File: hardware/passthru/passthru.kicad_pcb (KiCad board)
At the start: 2 copper layers, 63.5 x 59.7 mm, 83 parts, among them J1 ARM_SWD, J2 RJ45_LED_Shielded, J3 Screw_Terminal_01x02, Q1 Q_PMOS_DGS, Q2 Q_PMOS_DGS, Q3 Q_NPN_BEC, U1 EFM32GG11B8xx, U2 KSZ8081RND, U3 LM5085, U4 TPS2375-1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

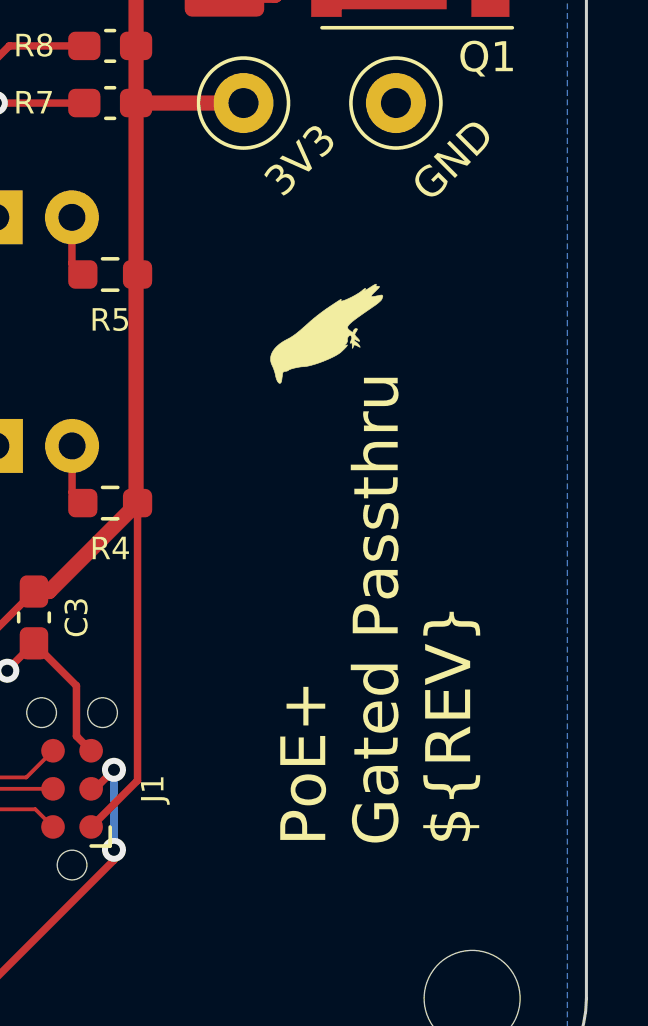
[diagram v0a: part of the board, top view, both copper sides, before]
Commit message: passthru: add pre-release revision to board
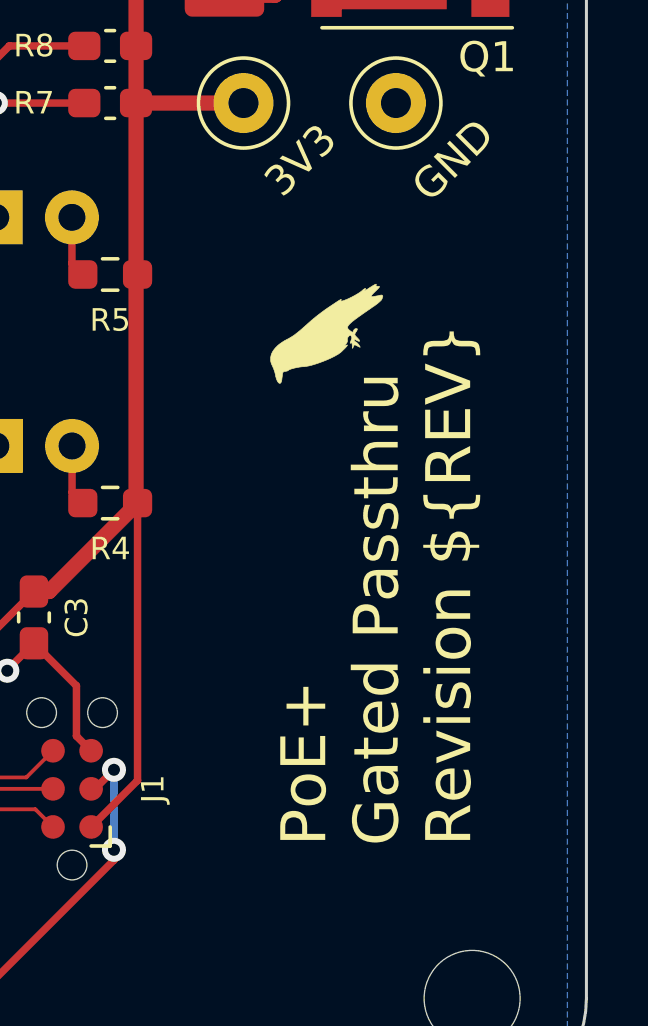
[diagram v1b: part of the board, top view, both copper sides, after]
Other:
- board text added: "PoE+ Gated Passthru Revision ${REV}"
- board text removed: "PoE+ Gated Passthru ${REV}"
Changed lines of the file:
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@@
     )
   )
+  (property "REV" "A-dev")
   (net 0 "")
   (net 1 "VDDA")
@@
     (effects (font (size 1 1) (thickness 0.2)) (justify mirror))
   )
-  (gr_text "PoE+\nGated Passthru\n${REV}" (at 170.815 112.395 90) (layer "F.SilkS")
+  (gr_text "PoE+\nGated Passthru\nRevision ${REV}" (at 170.815 112.395 90) (layer "F.SilkS")
     (effects (font (size 1.5 1.5) (thickness 0.3)) (justify left))
   )

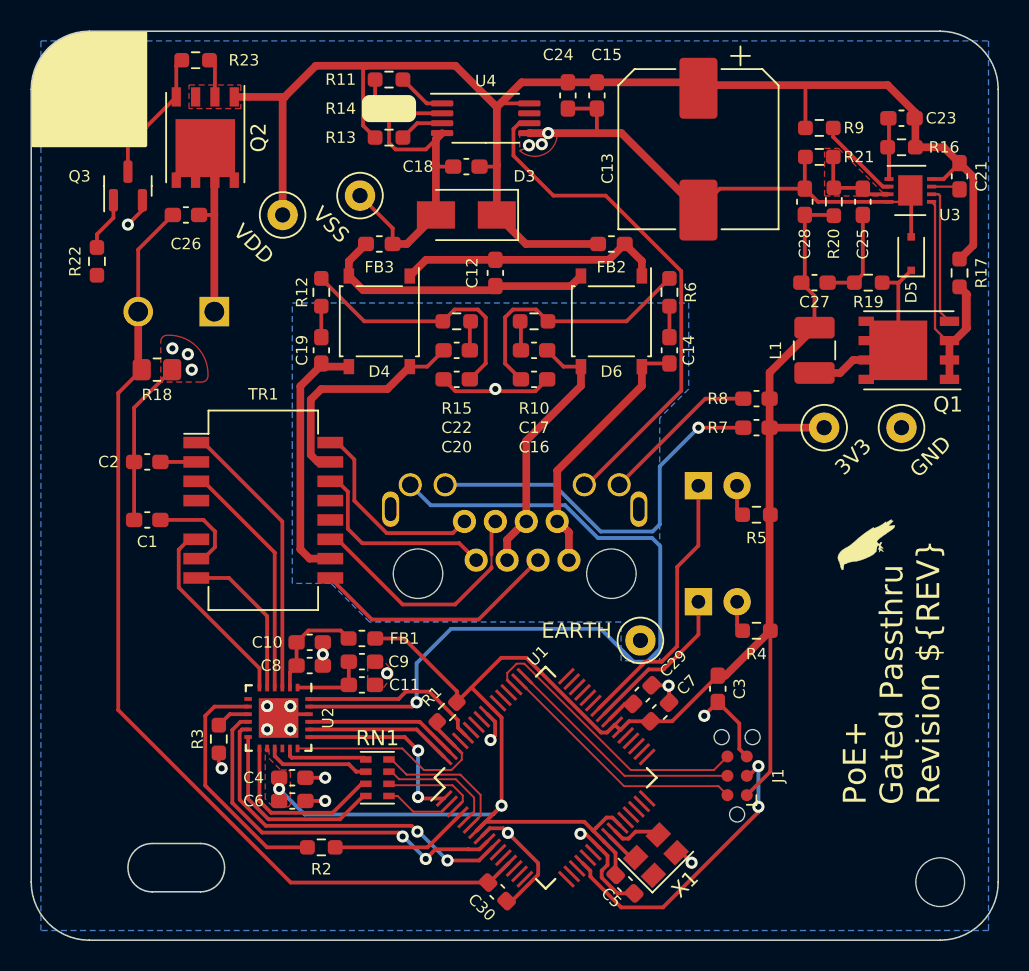
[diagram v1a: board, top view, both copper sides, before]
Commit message: passthru: finalize production parameters
I also spaced out the VDD rail a bit further.
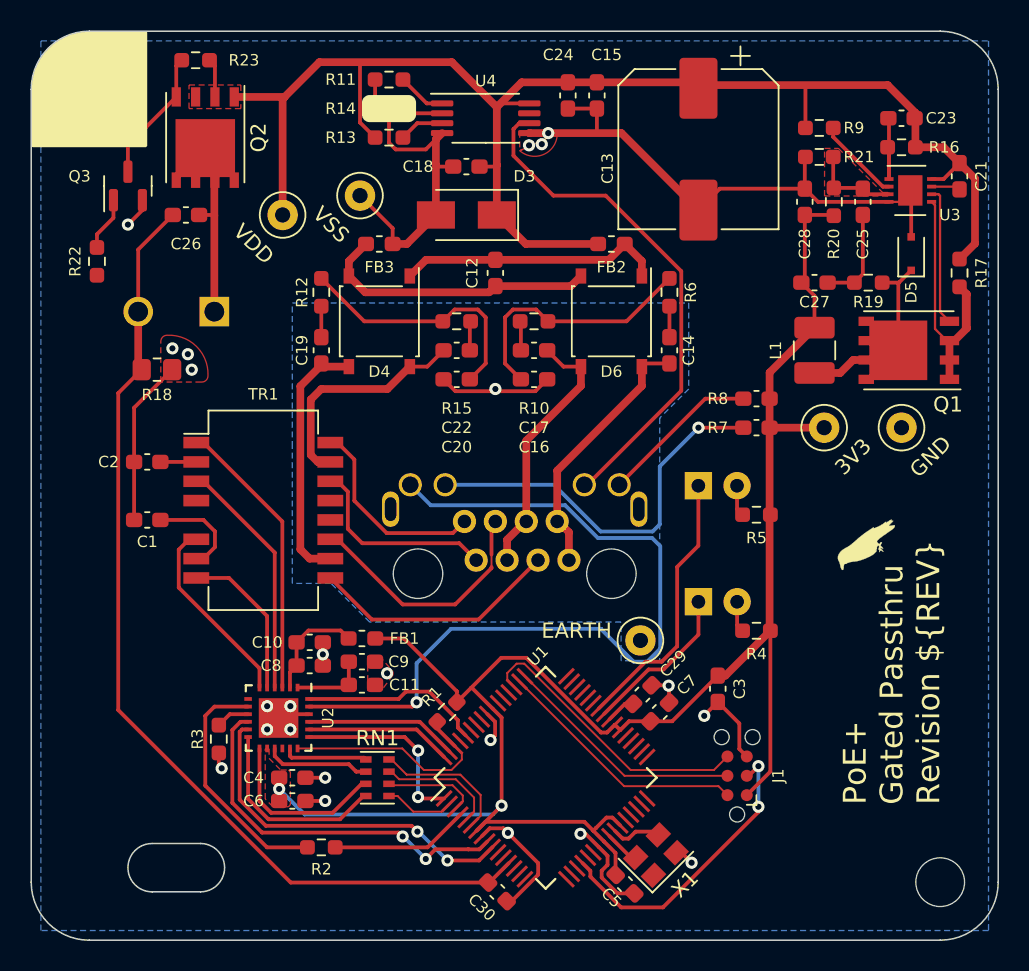
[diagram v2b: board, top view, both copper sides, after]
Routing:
- net VDD: track 99.7 -> 99.1 mm
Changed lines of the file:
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@@
 (kicad_pcb (version 20211014) (generator pcbnew)
   (general
-    (thickness 1.6)
+    (thickness 1.69)
   )
   (paper "A4")
@@
   (setup
     (stackup
-      (layer "F.SilkS" (type "Top Silk Screen"))
+      (layer "F.SilkS" (type "Top Silk Screen") (color "White"))
       (layer "F.Paste" (type "Top Solder Paste"))
-      (layer "F.Mask" (type "Top Solder Mask") (thickness 0.01))
+      (layer "F.Mask" (type "Top Solder Mask") (color "#0C4AD9D4") (thickness 0.01))
       (layer "F.Cu" (type "copper") (thickness 0.035))
-      (layer "dielectric 1" (type "core") (thickness 1.51) (material "FR4") (epsilon_r 4.5) (loss_tangent 0.02))
+      (layer "dielectric 1" (type "core") (thickness 1.6) (material "FR4") (epsilon_r 4.5) (loss_tangent 0.02))
       (layer "B.Cu" (type "copper") (thickness 0.035))
-      (layer "B.Mask" (type "Bottom Solder Mask") (thickness 0.01))
+      (layer "B.Mask" (type "Bottom Solder Mask") (color "#0C4AD9D4") (thickness 0.01))
       (layer "B.Paste" (type "Bottom Solder Paste"))
-      (layer "B.SilkS" (type "Bottom Silk Screen"))
+      (layer "B.SilkS" (type "Bottom Silk Screen") (color "White"))
       (copper_finish "None")
       (dielectric_constraints no)
@@
   (segment (start 139.16 77.67) (end 140.2225 76.6075) (width 0.508) (layer "F.Cu") (net 1))
   (segment (start 154.4 76.69) (end 153.275 75.565) (width 0.508) (layer "F.Cu") (net 1))
-  (segment (start 144.5107 78.6018) (end 144.78 78.3325) (width 0.508) (layer "F.Cu") (net 2))
   (segment (start 149.7375 78.3325) (end 150.4 77.67) (width 0.508) (layer "F.Cu") (net 2))
-  (segment (start 136.0918 78.6018) (end 144.5107 78.6018) (width 0.508) (layer "F.Cu") (net 2))
+  (segment (start 135.16 77.67) (end 136.23 78.74) (width 0.508) (layer "F.Cu") (net 2))
   (segment (start 135.16 76.69) (end 136.285 75.565) (width 0.508) (layer "F.Cu") (net 2))
   (segment (start 144.78 78.3325) (end 149.7375 78.3325) (width 0.508) (layer "F.Cu") (net 2))
   (segment (start 135.16 77.67) (end 135.16 76.69) (width 0.508) (layer "F.Cu") (net 2))
-  (segment (start 135.16 77.67) (end 136.0918 78.6018) (width 0.508) (layer "F.Cu") (net 2))
+  (segment (start 136.23 78.74) (end 144.3725 78.74) (width 0.508) (layer "F.Cu") (net 2))
+  (segment (start 144.3725 78.74) (end 144.78 78.3325) (width 0.508) (layer "F.Cu") (net 2))
   (segment (start 152.146 116.336876) (end 151.75875 116.724126) (width 0.25) (layer "F.Cu") (net 3))
   (segment (start 144.760877 107.842123) (end 144.4625 108.1405) (width 0.25) (layer "F.Cu") (net 3))
@@
   (segment (start 132.541 106.445) (end 131.591 106.445) (width 0.25) (layer "F.Cu") (net 3))
   (segment (start 149.5425 66.675) (end 151.4475 66.675) (width 0.25) (layer "F.Cu") (net 3))
-  (segment (start 157.00689 115.537901) (end 156.646825 115.537901) (width 0.25) (layer "F.Cu") (net 3))
   (segment (start 143.892392 114.453054) (end 144.407323 113.938123) (width 0.25) (layer "F.Cu") (net 3))
   (segment (start 151.564501 115.160161) (end 150.70434 114.3) (width 0.25) (layer "F.Cu") (net 3))
@@
   (via (at 144.78 85.09) (size 0.8) (drill 0.4) (layers "F.Cu" "B.Cu") (free) (net 4))
   (segment (start 174.2165 71.301) (end 175.26 70.2575) (width 0.25) (layer "F.Cu") (net 5))
+  (segment (start 176.276 75.5415) (end 175.26 76.5575) (width 0.508) (layer "F.Cu") (net 5))
   (segment (start 174.2175 69.215) (end 175.26 70.2575) (width 0.508) (layer "F.Cu") (net 5))
-  (segment (start 142.1582 63.8632) (end 144.875 66.58) (width 0.508) (layer "F.Cu") (net 5))
+  (segment (start 130.94 65.91) (end 133.223 63.627) (width 0.508) (layer "F.Cu") (net 5))
   (segment (start 126.0075 63.5) (end 126.365 63.8575) (width 0.25) (layer "F.Cu") (net 5))
   (segment (start 143.7375 70.485) (end 144.78 70.485) (width 0.25) (layer "F.Cu") (net 5))
   (segment (start 130.81 73.66) (end 130.81 66.04) (width 0.508) (layer "F.Cu") (net 5))
-  (segment (start 176.1668 75.6507) (end 175.26 76.5575) (width 0.508) (layer "F.Cu") (net 5))
-  (segment (start 136.2532 63.8632) (end 142.1582 63.8632) (width 0.508) (layer "F.Cu") (net 5))
+  (segment (start 176.276 71.2735) (end 176.276 75.5415) (width 0.508) (layer "F.Cu") (net 5))
   (segment (start 158.3238 65.1332) (end 170.5432 65.1332) (width 0.508) (layer "F.Cu") (net 5))
   (segment (start 151.4475 64.95) (end 157.723 64.95) (width 0.508) (layer "F.Cu") (net 5))
-  (segment (start 175.26 70.2575) (end 175.989 70.9865) (width 0.1524) (layer "F.Cu") (net 5))
-  (segment (start 136.0922 64.0242) (end 136.2532 63.8632) (width 0.25) (layer "F.Cu") (net 5))
-  (segment (start 136.8825 68.58) (end 136.0922 67.7897) (width 0.25) (layer "F.Cu") (net 5))
   (segment (start 170.5432 65.1332) (end 172.3625 66.9525) (width 0.508) (layer "F.Cu") (net 5))
+  (segment (start 136.8825 68.58) (end 135.89 67.5875) (width 0.25) (layer "F.Cu") (net 5))
   (segment (start 130.81 66.04) (end 130.94 65.91) (width 0.508) (layer "F.Cu") (net 5))
   (segment (start 151.525 75.565) (end 146.78 75.565) (width 0.508) (layer "F.Cu") (net 5))
+  (segment (start 135.89 67.5875) (end 135.89 63.754) (width 0.25) (layer "F.Cu") (net 5))
   (segment (start 173.427 71.301) (end 174.2165 71.301) (width 0.25) (layer "F.Cu") (net 5))
   (segment (start 147.0075 66.335) (end 145.12 66.335) (width 0.25) (layer "F.Cu") (net 5))
   (segment (start 149.5425 64.95) (end 146.505 64.95) (width 0.508) (layer "F.Cu") (net 5))
+  (segment (start 175.26 70.2575) (end 176.276 71.2735) (width 0.508) (layer "F.Cu") (net 5))
   (segment (start 144.875 66.58) (end 144.875 70.39) (width 0.508) (layer "F.Cu") (net 5))
   (segment (start 165.14 67.945) (end 165.14 65.1332) (width 0.25) (layer "F.Cu") (net 5))
-  (segment (start 175.26 70.2575) (end 176.1668 71.1643) (width 0.508) (layer "F.Cu") (net 5))
   (segment (start 144.78 70.485) (end 144.875 70.39) (width 0.25) (layer "F.Cu") (net 5))
+  (segment (start 133.223 63.627) (end 141.922 63.627) (width 0.508) (layer "F.Cu") (net 5))
   (segment (start 146.505 64.95) (end 144.875 66.58) (width 0.508) (layer "F.Cu") (net 5))
+  (segment (start 141.922 63.627) (end 144.875 66.58) (width 0.508) (layer "F.Cu") (net 5))
   (segment (start 172.3625 69.215) (end 174.2175 69.215) (width 0.508) (layer "F.Cu") (net 5))
   (segment (start 146.78 75.565) (end 144.875 73.66) (width 0.508) (layer "F.Cu") (net 5))
   (segment (start 127.635 65.91) (end 130.94 65.91) (width 0.508) (layer "F.Cu") (net 5))
   (segment (start 172.3625 66.9525) (end 172.3625 69.215) (width 0.508) (layer "F.Cu") (net 5))
-  (segment (start 176.1668 71.1643) (end 176.1668 75.6507) (width 0.508) (layer "F.Cu") (net 5))
-  (segment (start 136.0922 67.7897) (end 136.0922 64.0242) (width 0.25) (layer "F.Cu") (net 5))
   (segment (start 149.5425 64.95) (end 151.4475 64.95) (width 0.508) (layer "F.Cu") (net 5))
   (segment (start 145.12 66.335) (end 144.875 66.58) (width 0.25) (layer "F.Cu") (net 5))
   (segment (start 126.365 63.8575) (end 126.365 65.91) (width 0.25) (layer "F.Cu") (net 5))
-  (segment (start 130.94 65.91) (end 132.9868 63.8632) (width 0.508) (layer "F.Cu") (net 5))
-  (segment (start 132.9868 63.8632) (end 136.2532 63.8632) (width 0.508) (layer "F.Cu") (net 5))
   (segment (start 144.875 70.39) (end 144.875 73.66) (width 0.508) (layer "F.Cu") (net 5))
   (segment (start 138.97 75.565) (end 140.875 73.66) (width 0.508) (layer "F.Cu") (net 6))
@@
   (segment (start 120.015 85.36) (end 121.555 83.82) (width 0.25) (layer "F.Cu") (net 9))
   (segment (start 121.325 75.9325) (end 123.5975 73.66) (width 0.25) (layer "F.Cu") (net 9))
-  (segment (start 121.325 83.59) (end 121.555 83.82) (width 0.508) (layer "F.Cu") (net 9))
   (segment (start 150.622268 113.510822) (end 151.207223 114.095777) (width 0.25) (layer "F.Cu") (net 10))
   (segment (start 153.557886 106.90888) (end 154.96512 106.90888) (width 0.25) (layer "F.Cu") (net 10))
@@
   (segment (start 152.625161 114.099501) (end 153.140093 114.614433) (width 0.25) (layer "F.Cu") (net 111))
   (segment (start 153.140093 114.614433) (end 153.528403 114.614433) (width 0.25) (layer "F.Cu") (net 111))
-  (segment (start 155.26471 114.155786) (end 155.480099 114.371175) (width 0.25) (layer "F.Cu") (net 111))
-  (segment (start 153.674653 115.856099) (end 153.995175 115.856099) (width 0.25) (layer "F.Cu") (net 112))
   (segment (start 152.271608 114.453054) (end 153.674653 115.856099) (width 0.25) (layer "F.Cu") (net 112))
   (segment (start 158.115 101.219) (end 158.115 99.06) (width 0.25) (layer "F.Cu") (net 114))

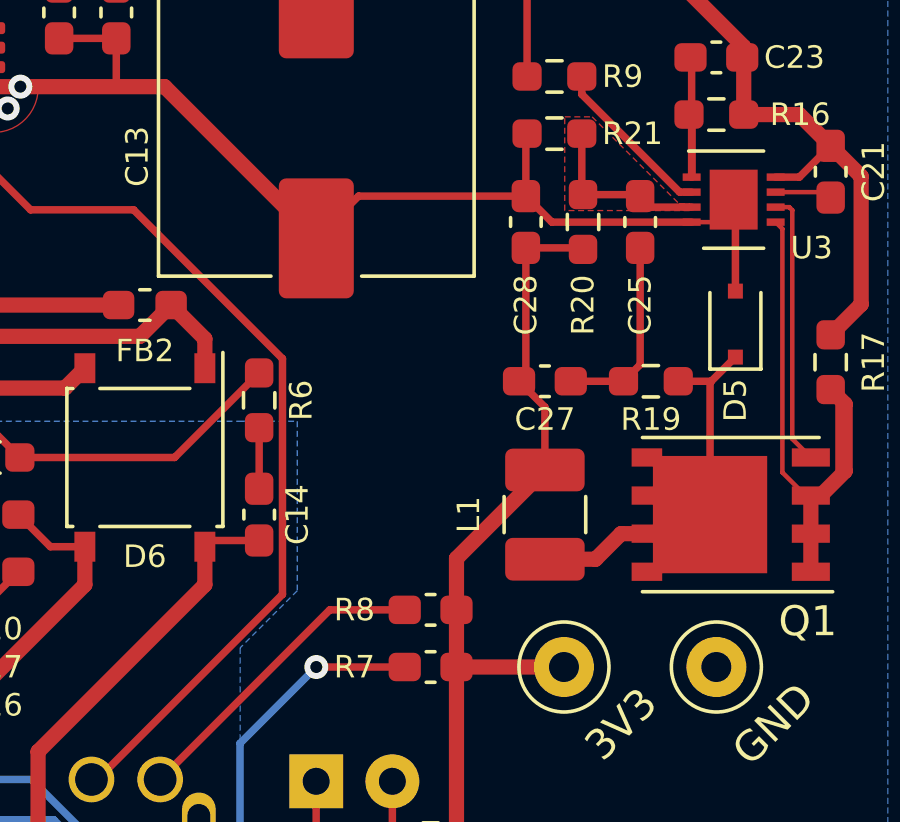
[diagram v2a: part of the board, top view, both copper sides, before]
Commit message: passthru: change package for C28
This is a larger-capacity capacitor.
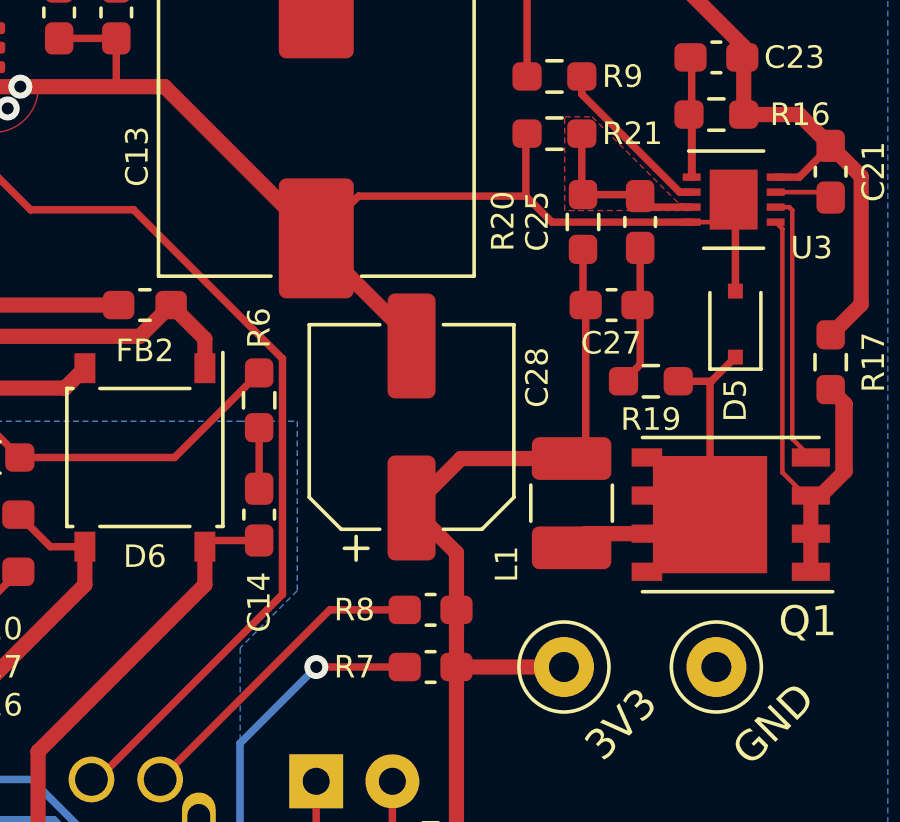
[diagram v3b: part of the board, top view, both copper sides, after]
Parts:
- C28: footprint Capacitor_SMD:C_0603_1608Metric_Pad1.08x0.95mm_HandSolder -> Capacitor_SMD:CP_Elec_6.3x5.8
- moved C28 7.82 mm to (161.3, 79.6)
- moved C27 3.38 mm to (168.0, 75.6)
- moved L1 0.97 mm to (166.6, 82.2)
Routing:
- net GND: track 81.0 -> 85.7 mm
- net +3V3: track 120.6 -> 122.5 mm
- net Net-(C25-Pad2): track 6.43 -> 4.68 mm
- net Net-(D5-Pad1): track 10.5 -> 9.41 mm

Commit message: passthru: increase the resistance of the VDD shunt resistor
Assuming a maximum VDD current of 600 mA, this will give a maximum
sense voltage of 0.6 V and 36 mW of power draw.
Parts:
- R18: value 10m -> 0R1
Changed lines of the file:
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@@
       (effects (font (size 0.75 0.75) (thickness 0.15)))
     )
-    (fp_text value "10m" (at 0 1.65) (layer "F.Fab")
+    (fp_text value "0R1" (at 0 1.65) (layer "F.Fab")
       (effects (font (size 1 1) (thickness 0.15)))
     )
